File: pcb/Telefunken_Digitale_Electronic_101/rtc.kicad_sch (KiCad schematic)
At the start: 5 parts, among them U1 DS3231

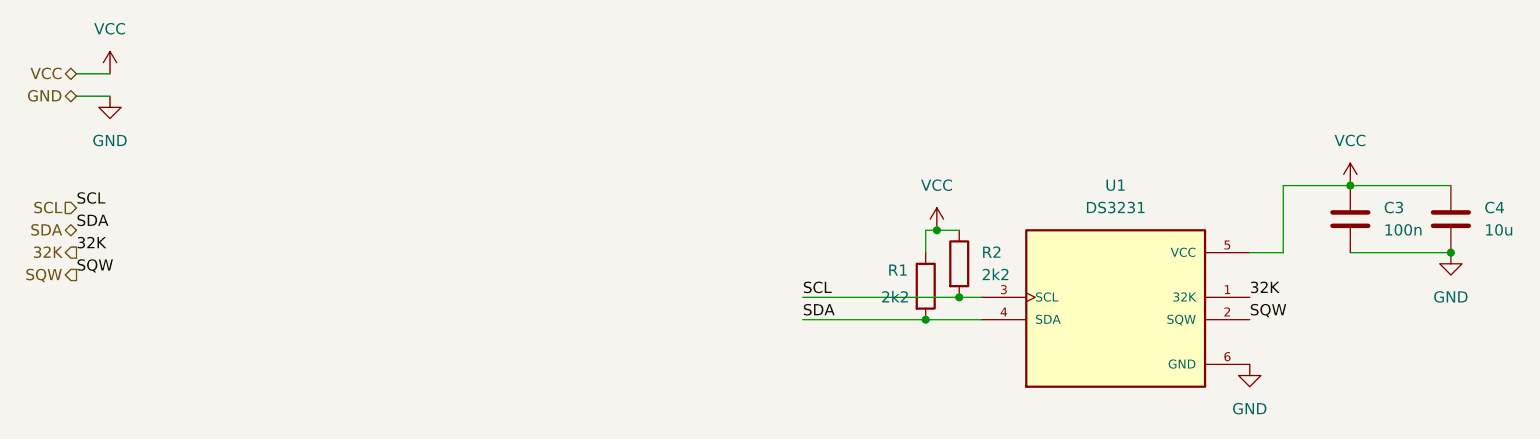
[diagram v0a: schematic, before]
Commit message: TFK: sch - i2c resistors not populate, logo; pcb - spaced tracks, stitching vias, logo
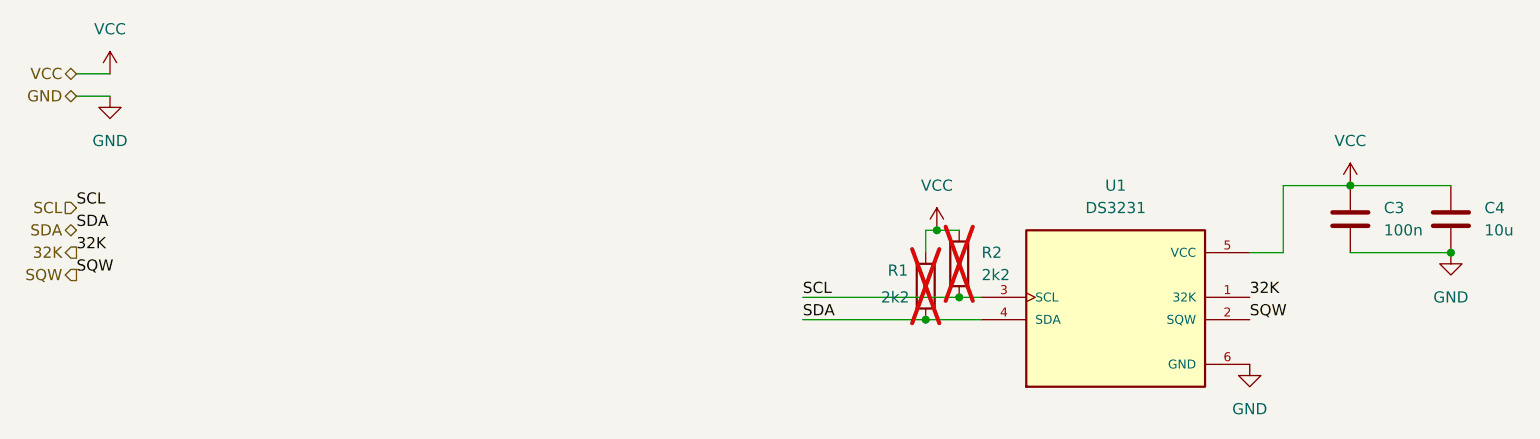
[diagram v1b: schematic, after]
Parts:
- R1, R2: now not fitted
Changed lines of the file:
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@@
 		(on_board yes)
 		(in_pos_files yes)
-		(dnp no)
+		(dnp yes)
 		(fields_autoplaced yes)
 		(property "Reference" "R2"
@@
 		(on_board yes)
 		(in_pos_files yes)
-		(dnp no)
+		(dnp yes)
 		(property "Reference" "R1"
 			(at 130.302 79.502 0)
